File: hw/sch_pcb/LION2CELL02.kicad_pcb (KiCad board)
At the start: 2 copper layers, 80.8 x 60.5 mm, 88 parts, among them J1 USBC_USB4105-GF-A, J10 HEADER_2x01_PARALLEL, J11 HEADER_1x02, J12 HEADER_2x05_PARALLEL, J2 CONN1_1, J3 CONN1_1, J4 JUMP_4X2, J6 HEADER_2x01_PARALLEL, J7 HEADER_2x01_PARALLEL, J8 CONN1_1, J9 CONN1_1, Q1 DMT31M7LPS, Q2 AP2305AGN-HF-3, Q3 DMT31M7LPS, Q5 DMT31M7LPS, SW1 SW_Push, SW2 SW_Push, U1 BQ25792RQMR1, U3 BQ40z50-R2

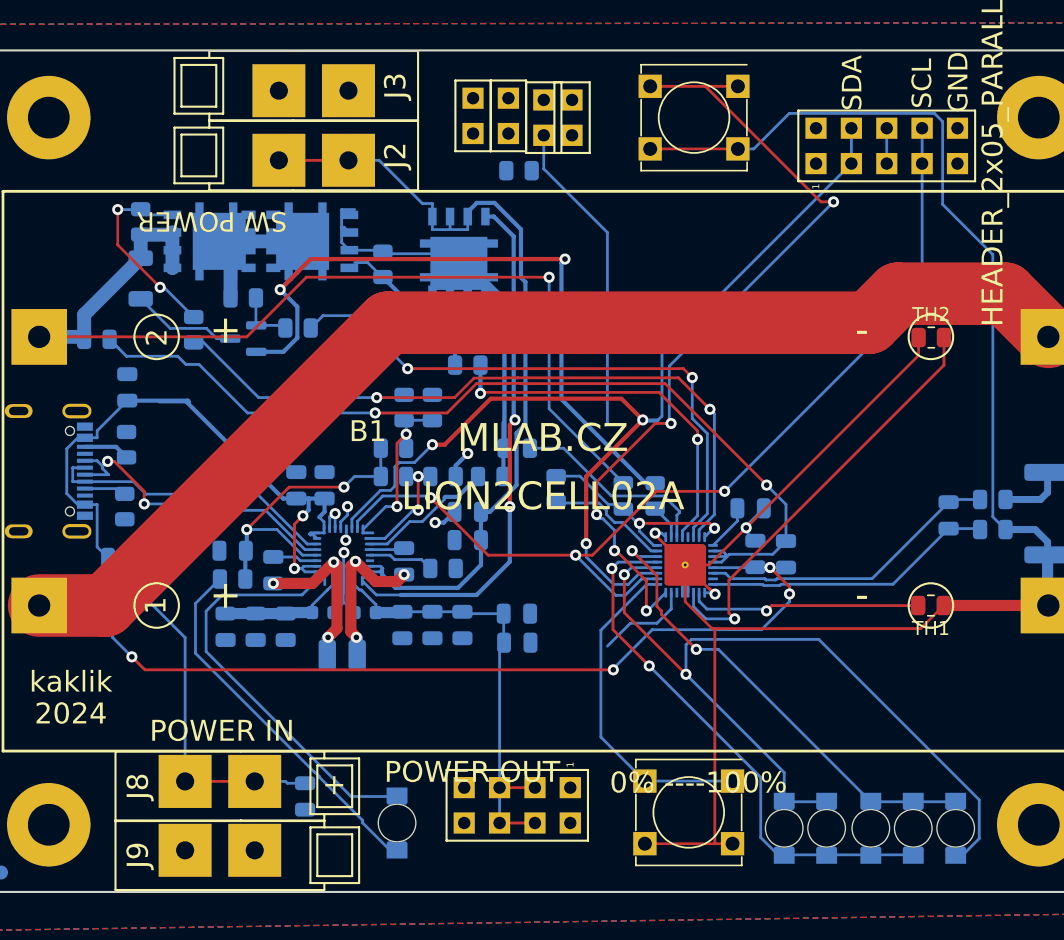
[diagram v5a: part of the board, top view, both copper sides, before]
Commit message: The first completely routed nets.
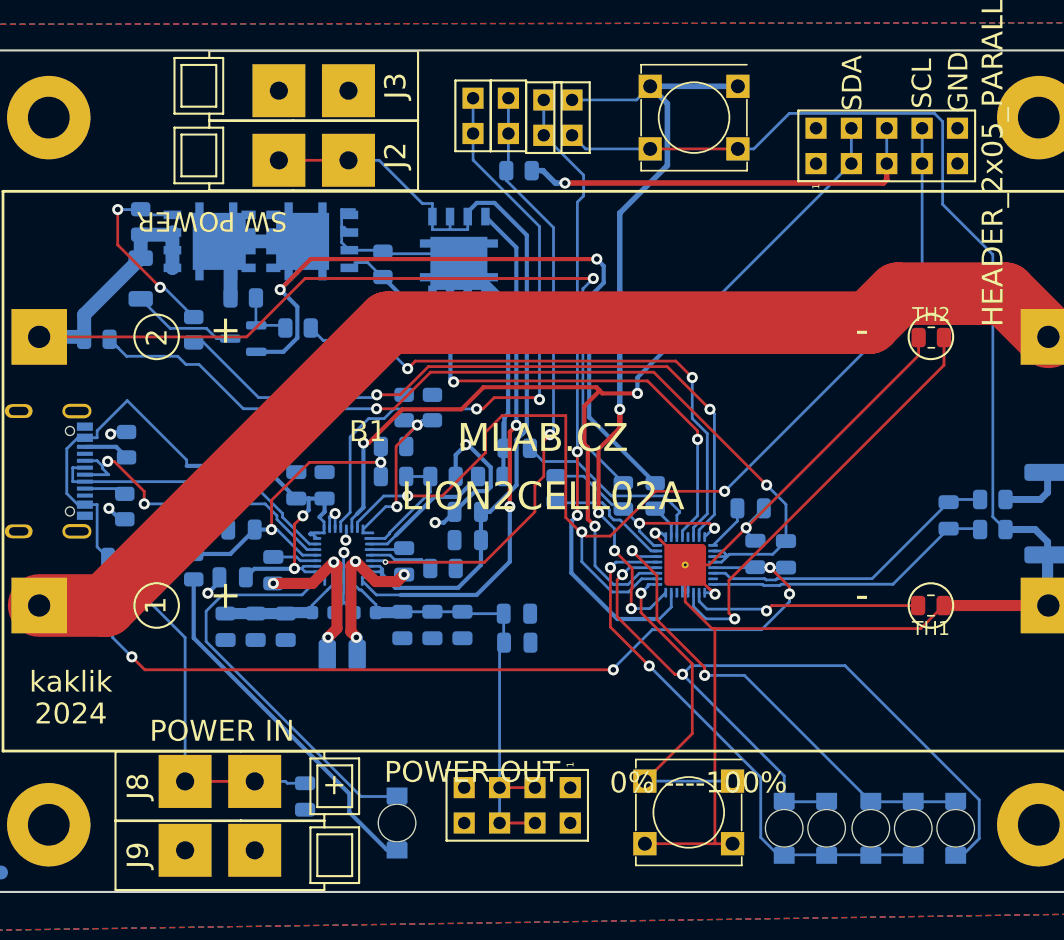
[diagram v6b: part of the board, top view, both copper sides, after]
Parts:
- moved C4 15.6 mm to (126.1, 112.6), turned to 180 degrees
- moved R27 3.63 mm to (140.9, 94.5)
- moved R7 2.93 mm to (123.4, 111.9), turned to -90 degrees
- moved C20 1.65 mm to (126.8, 109.2)
- moved R5 0.13 mm to (137.7, 103.2)
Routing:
- net Net-(U1-INT): track 0.00 -> 44.9 mm, vias 0 -> 2
- net Net-(U1-nQON): track 1.79 -> 45.3 mm, vias 1 -> 2
- net +3.3V: track 2.54 -> 29.7 mm, vias 0 -> 1
- net Net-(U3-BTP_INT): track 29.7 -> 45.5 mm, vias 0 -> 2
- net GND: track 17.4 -> 28.8 mm, vias 5 -> 8
- net /Fuel Gauge/SDA: track 71.1 -> 80.9 mm
- net GND1: track 153.4 -> 159.4 mm
- net Net-(U3-DSG): track 26.9 -> 31.3 mm
- net Net-(Q5-G): track 10.9 -> 6.68 mm
- net Net-(U3-~{PRES/SHDWN}): track 59.9 -> 56.4 mm, vias 5 -> 4
- net /Fuel Gauge/B+: track 72.8 -> 75.1 mm
- net /Power Input/REGN: track 22.5 -> 24.6 mm
- net Net-(D1-A): track 59.2 -> 57.5 mm
- net /Fuel Gauge/VCOM: track 61.0 -> 62.5 mm
- net Net-(U1-TS): track 13.5 -> 14.7 mm
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
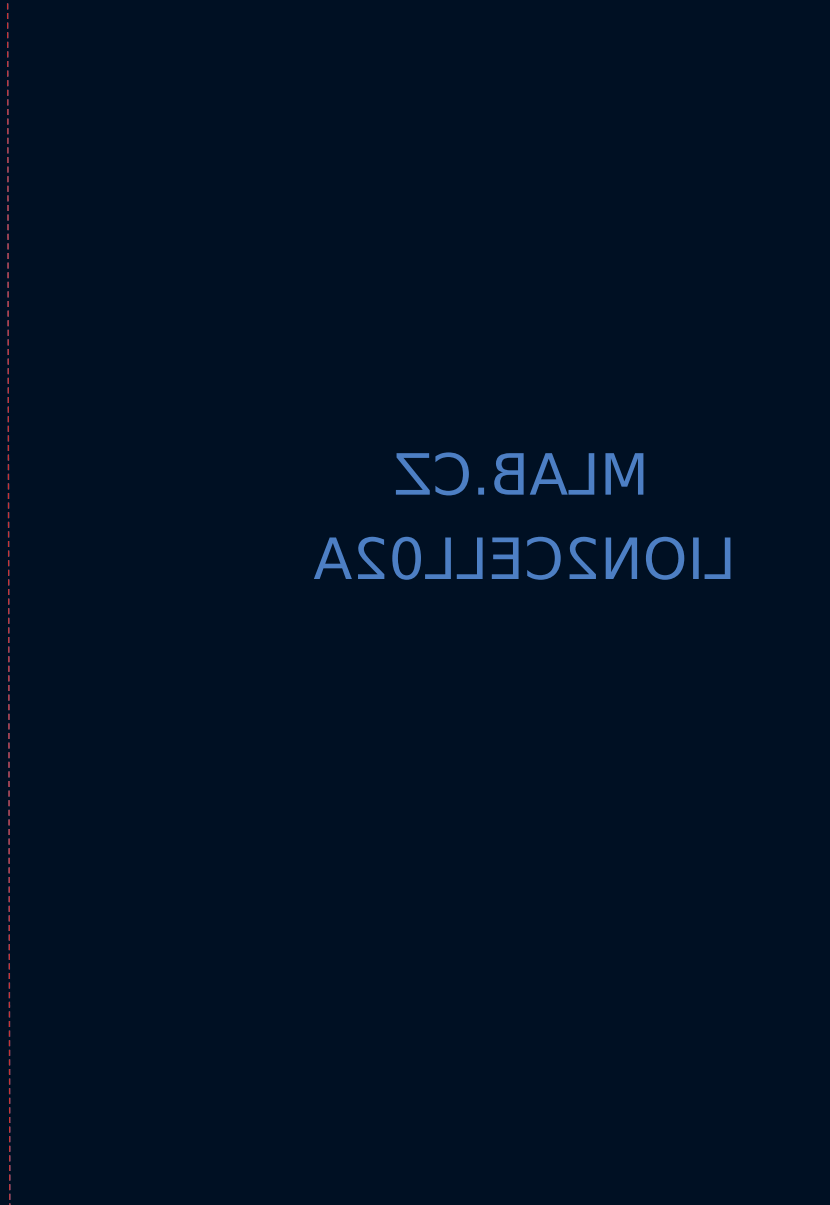
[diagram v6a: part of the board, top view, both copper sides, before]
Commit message: Adding output voltage switching regulator.
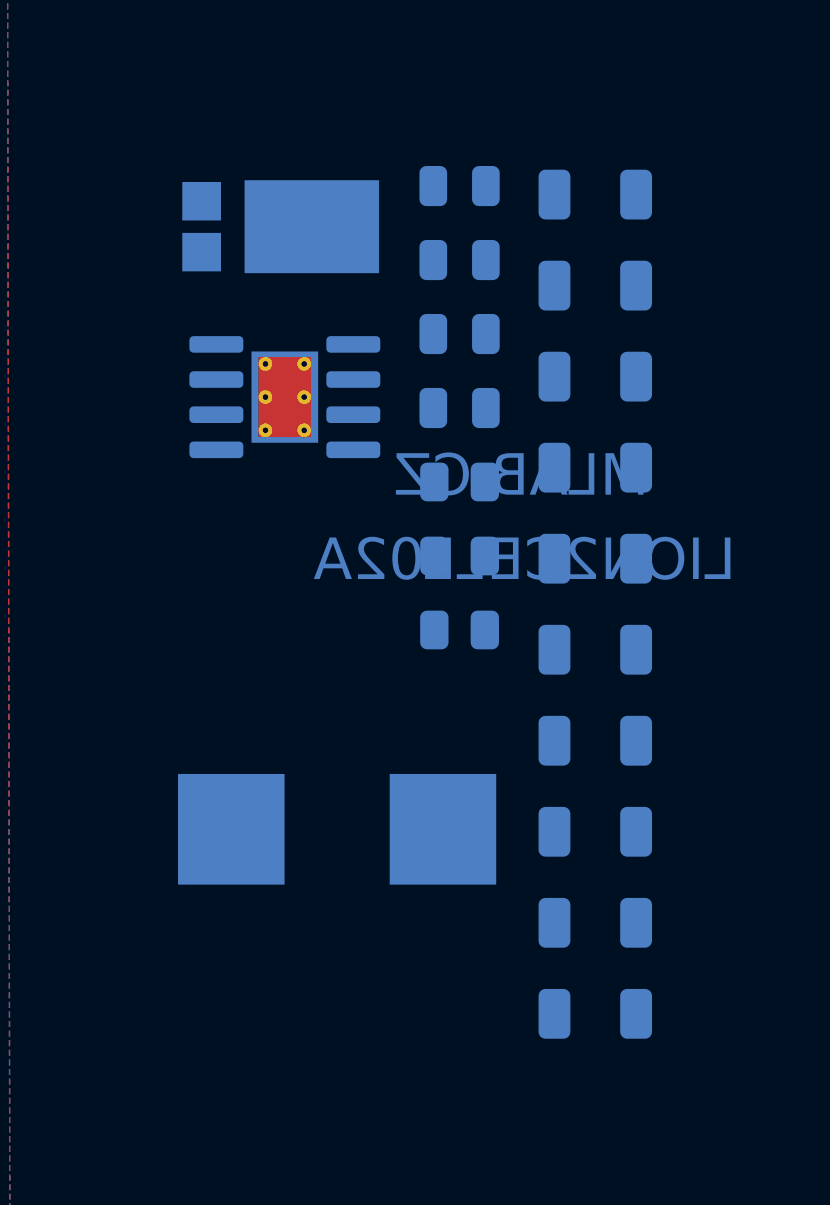
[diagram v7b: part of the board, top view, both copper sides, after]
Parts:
- added C12: 10uF/50V, Capacitor_SMD:C_1206_3216Metric, B.Cu at (212.8, 91.1)
- added C13: 10uF/50V, Capacitor_SMD:C_1206_3216Metric, B.Cu at (212.8, 94.4)
- added C14: 10uF/50V, Capacitor_SMD:C_1206_3216Metric, B.Cu at (212.8, 97.7)
- added C15: 10uF/50V, Capacitor_SMD:C_1206_3216Metric, B.Cu at (212.8, 101.0)
- added C22: 100nF/50V, Capacitor_SMD:C_0805_2012Metric, B.Cu at (207.9, 90.8)
- added C23: 100nF, Capacitor_SMD:C_0805_2012Metric, B.Cu at (207.9, 93.5)
- added C28: 10uF/50V, Capacitor_SMD:C_1206_3216Metric, B.Cu at (212.8, 104.3)
- added C32: 10uF/50V, Capacitor_SMD:C_1206_3216Metric, B.Cu at (212.8, 107.6)
- added C33: 10uF/50V, Capacitor_SMD:C_1206_3216Metric, B.Cu at (212.8, 110.9)
- added C34: 10uF/50V, Capacitor_SMD:C_1206_3216Metric, B.Cu at (212.8, 114.2)
- added C35: 1uF, Capacitor_SMD:C_0805_2012Metric, B.Cu at (207.9, 96.2)
- added C36: 100uF/6V3, Capacitor_SMD:C_1206_3216Metric, B.Cu at (212.8, 117.5)
- added C37: 100uF/6V3, Capacitor_SMD:C_1206_3216Metric, B.Cu at (212.8, 120.8)
- added C38: 22nF, Capacitor_SMD:C_0805_2012Metric, B.Cu at (207.9, 98.9)
- added D2: PDS760-13, Diode_SMD:D_PowerDI-5, B.Cu at (201.5, 92.3)
- added L2: HCI1050-5R5, Inductor_SMD:L_Wuerth_HCI-1050, B.Cu at (203.5, 114.1)
- added R10: 91k, Resistor_SMD:R_0805_2012Metric, B.Cu at (207.9, 101.5)
- added R12: 59kR, Resistor_SMD:R_0805_2012Metric, B.Cu at (207.9, 104.2)
- added R13: 15k, Resistor_SMD:R_0805_2012Metric, B.Cu at (207.9, 106.9)
- added U2: LMR14050, Package_SO:SOIC-8-1EP_3.9x4.9mm_P1.27mm_EP2.41x3.3mm_ThermalVias, B.Cu at (201.6, 98.5)
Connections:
- H1 pad 1: GND -> unconnected-(H1-Pad1)
- H2 pad 1: GND -> unconnected-(H2-Pad1)
- H3 pad 1: GND -> unconnected-(H3-Pad1)
- H4 pad 1: GND -> unconnected-(H4-Pad1)

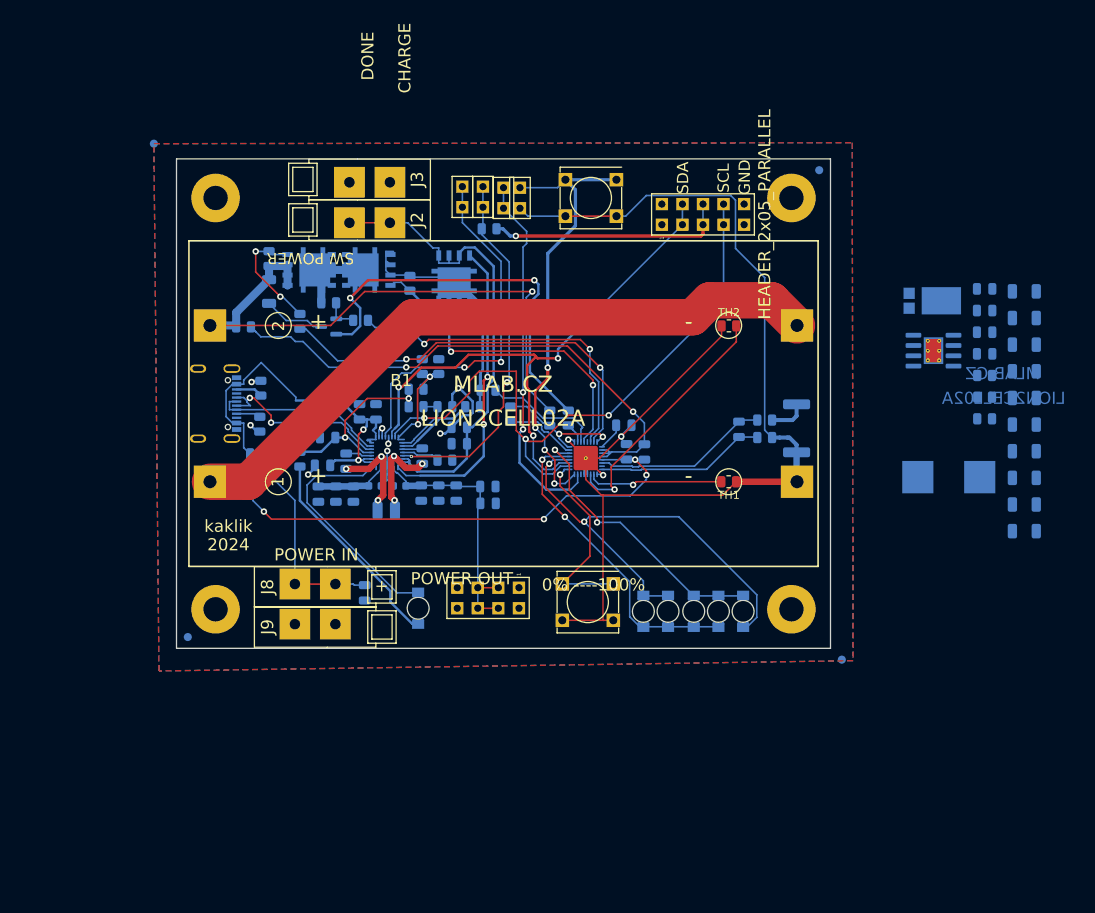
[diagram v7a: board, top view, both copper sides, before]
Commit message: Minimizing output regulator components count.
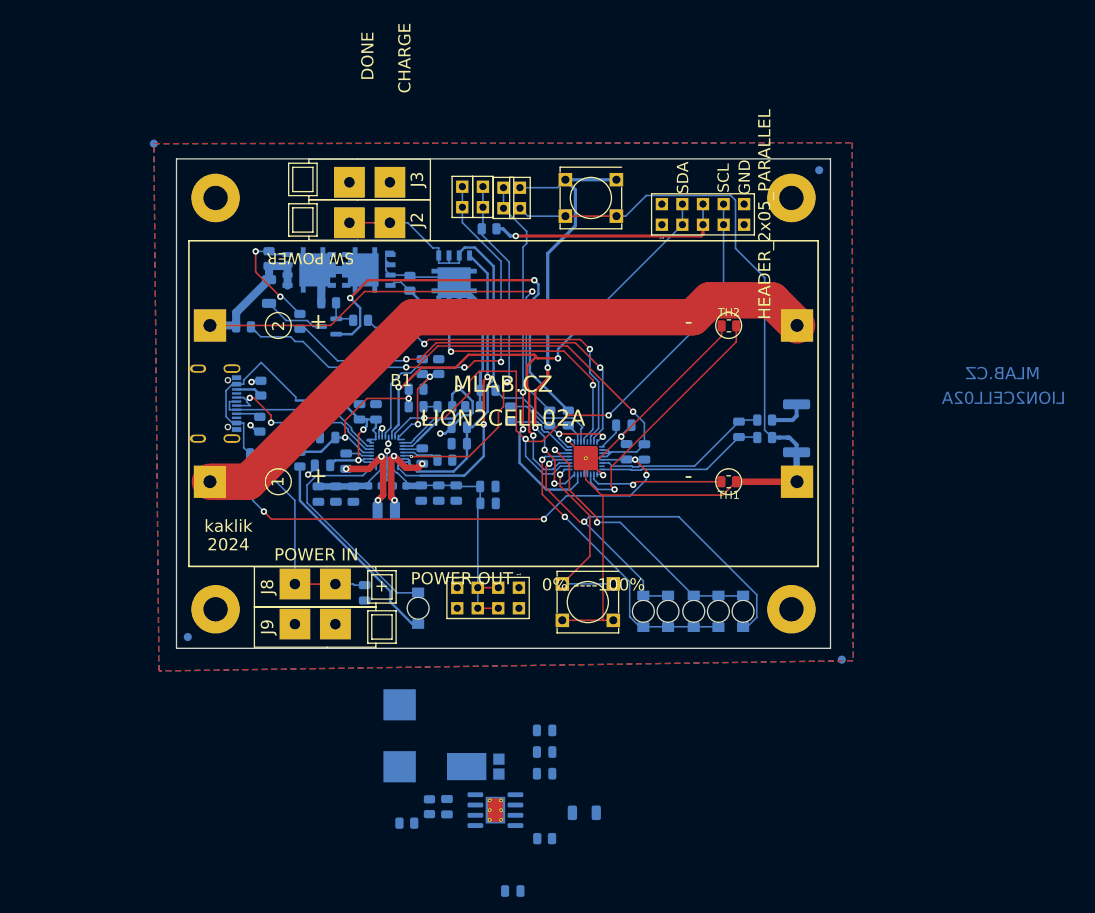
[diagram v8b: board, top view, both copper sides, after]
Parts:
- removed C12, C13, C14, C28, C32, C33, C34: 10uF/50V, Capacitor_SMD:C_1206_3216Metric
- removed C37: 100uF/6V3, Capacitor_SMD:C_1206_3216Metric
- C15: value 10uF/50V -> 10uF
- C22: value 100nF/50V -> 100nF
- C36: value 100uF/6V3 -> 10uF; footprint Capacitor_SMD:C_1206_3216Metric -> Capacitor_SMD:C_0805_2012Metric
- R12: value 59kR -> 59k
- moved R10 90.3 mm to (136.6, 156.8), turned to 0 degrees
- moved C38 86.8 mm to (141.5, 154.8), turned to 90 degrees
- moved R13 83.6 mm to (139.4, 154.8), turned to 90 degrees
- moved D2 80.6 mm to (145.1, 149.8), turned to 0 degrees
- moved C36 79.2 mm to (149.6, 165.2)
- moved U2 78.4 mm to (147.5, 155.2)
- moved C15 77.0 mm to (158.5, 155.5)
- moved C22 77.0 mm to (153.6, 145.4)
- moved C23 77.0 mm to (153.6, 148.0)
- moved R12 77.0 mm to (153.6, 158.7)
- moved C35 77.0 mm to (153.6, 150.7)
- moved L2 75.0 mm to (135.7, 146.0), turned to 90 degrees
